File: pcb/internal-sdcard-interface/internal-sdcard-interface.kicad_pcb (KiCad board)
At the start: 2 copper layers, 219 x 88 mm, 77 parts, among them J1 EXPANSION BOARD, J2 POWER, J3 TERMINAL, J5 SDCARD, U1 74HC04, U10 74HC173, U11 74HC245, U12 74HC157, U17 74HC85, U18 74HC00, U19 74HC00, U2 CY62256-70PC, U20 74HC02, U21 74HC123, U23 74HC163, U24 74HC138, U25 74HC138, U26 74HC32, U27 74HC00, U29 74HC165, U3 74HC00, U30 74HC595, U31 74HC273, U32 74HC273, U33 SST39SF010, U34 CY62128ELL-45SXI, U4 CY62256-70PC, U5 74HC74, U6 74HC74, U7 74HC32, U8 74HC688, U9 74HC32, X1 16MHz

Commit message: Updating session
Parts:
- added G***: LOGO, components:hcm_logo, F.Cu at (253.2, 133.1)
- moved C10 10.9 mm to (130.8, 122.0), turned to -90 degrees
- moved J2 2.79 mm to (254.0, 85.1), turned to 0 degrees
- moved C3 2.29 mm to (67.3, 123.2)
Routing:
- net D0: track 0.00 -> 414.0 mm, vias 0 -> 5
- net D1: track 0.00 -> 384.9 mm, vias 0 -> 4
- net ~{WR}: track 0.00 -> 360.9 mm, vias 0 -> 2
- net D2: track 0.00 -> 332.0 mm, vias 0 -> 1
- net D6: track 0.00 -> 293.3 mm, vias 0 -> 2
- net ~{RES}: track 0.00 -> 292.3 mm, vias 0 -> 4
- net ~{RD}: track 0.00 -> 277.3 mm, vias 0 -> 2
- net D3: track 0.00 -> 275.8 mm, vias 0 -> 4
- net D4: track 0.00 -> 271.4 mm, vias 0 -> 2
- net D7: track 0.00 -> 265.1 mm, vias 0 -> 3
- net D5: track 0.00 -> 251.5 mm, vias 0 -> 2
- net Net-(U6B-C): track 0.00 -> 229.5 mm, vias 0 -> 3
- net Net-(U6A-C): track 0.00 -> 227.3 mm, vias 0 -> 4
- net CA15: track 0.00 -> 223.5 mm, vias 0 -> 3
- net A3: track 0.00 -> 221.9 mm, vias 0 -> 2
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- added copper zone on F.Cu, net GND
- added copper zone on B.Cu, net VCC
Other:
- board text added: "SDRE - MINIBOARD rev0 SD-CARD INTERFACE / 64 KiB - RAM-EXPANSION"
- board text removed: "MINIBOARD SD-CARD INTERFACE / 64 KiB - RAM-EXPANSION"

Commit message: Finalizing rev0
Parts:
- added REF**: OSHW-Logo2_7.3x6mm_SilkScreen, Symbol:OSHW-Logo2_7.3x6mm_SilkScreen, F.Cu at (253.5, 125.0)
- moved C10 12.1 mm to (135.6, 133.1), turned to 0 degrees
- moved C3 3.22 mm to (65.4, 125.7)
- renumbered G*** to G001
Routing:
- net GND: track 1846.3 -> 1693.2 mm, vias 2 -> 7
- net Net-(U6B-C): track 229.5 -> 202.7 mm, vias 3 -> 5
- net D0: track 414.0 -> 432.2 mm, vias 5 -> 4
- net VCC: track 1411.9 -> 1421.2 mm, vias 0 -> 1
- net CLK: track 124.2 -> 133.3 mm, vias 3 -> 5
- net CA6: track 193.5 -> 189.6 mm
- net ~{CLKSTART_DB}: track 137.4 -> 139.8 mm
- net CA4: track 169.0 -> 171.0 mm
- net RAMS2: track 158.1 -> 160.1 mm, vias 1 -> 3
- net CA10: track 172.6 -> 174.2 mm
- net CA13: track 198.4 -> 199.9 mm
- net CA11: track 191.3 -> 192.7 mm
- net CA8: track 190.5 -> 189.1 mm
- net ~{S13}: track 181.6 -> 182.9 mm
- net A14: track 170.3 -> 171.5 mm, vias 1 -> 3
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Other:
- board text added: "CLK"
- board text added: "Designed by Ivo Filot (2024) Sources: https://github.com/ifilot/p2000t-sdcard"
- board text added: "LEDBANK"
- board text added: "MISO"
- board text added: "MOSI"
- board text added: "VCC"
- board text added: "~{CS}"

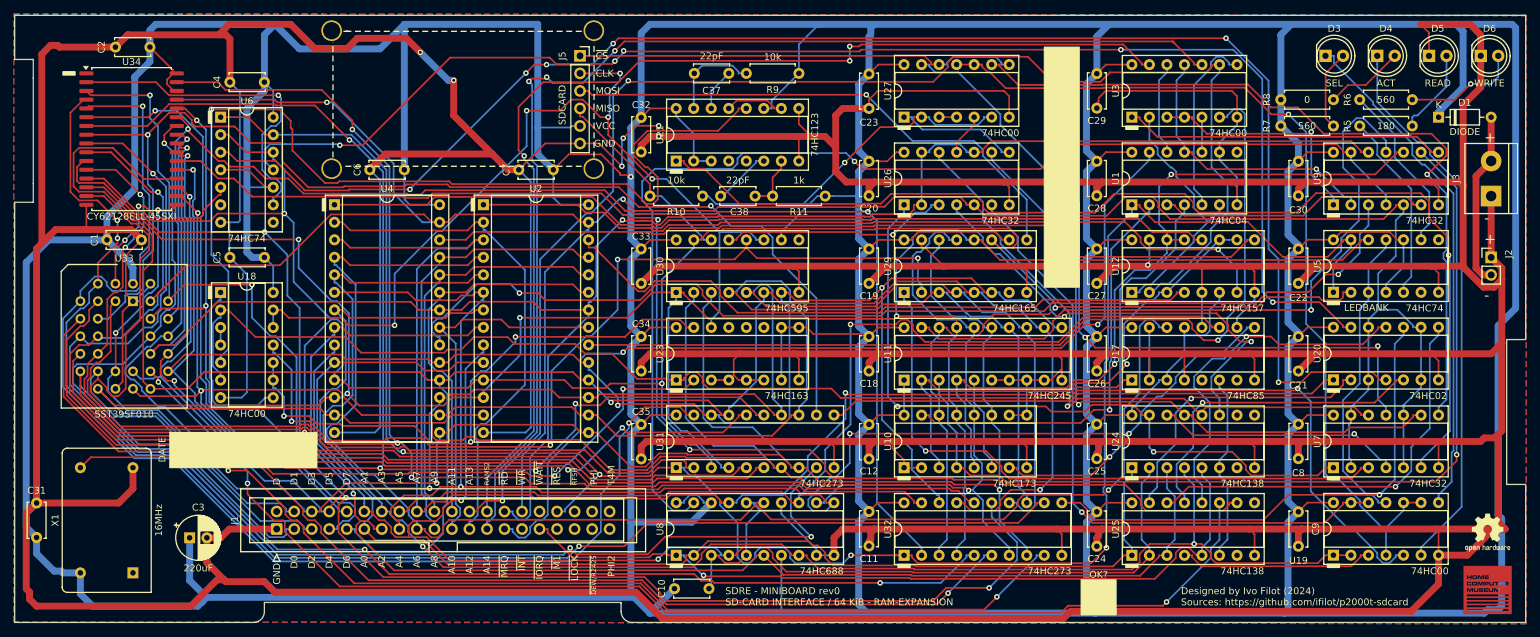
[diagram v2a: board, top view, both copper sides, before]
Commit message: Small revision of miniboard and enabling autoboot function
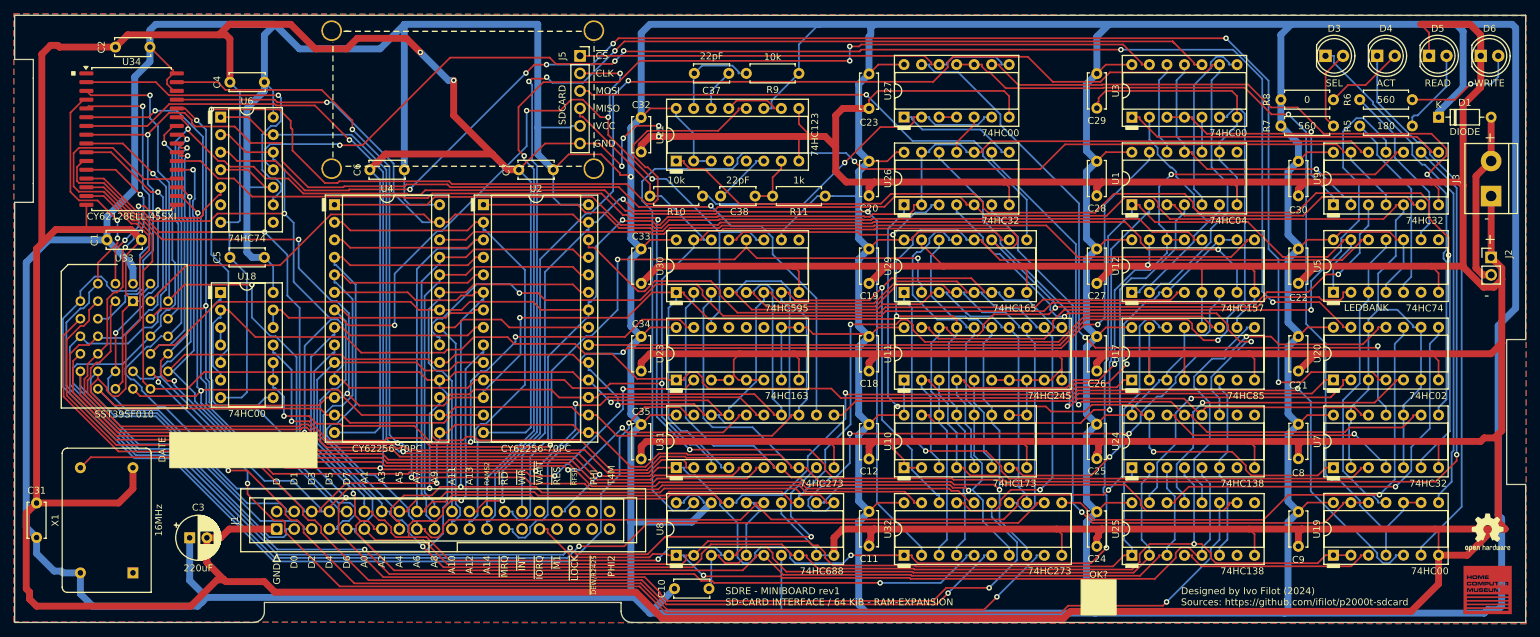
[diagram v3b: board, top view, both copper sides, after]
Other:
- board text added: "SDRE - MINIBOARD rev1 SD-CARD INTERFACE / 64 KiB - RAM-EXPANSION"
- board text removed: "SDRE - MINIBOARD rev0 SD-CARD INTERFACE / 64 KiB - RAM-EXPANSION"
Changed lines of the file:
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@@
 		(tags "THT DIP DIL PDIP 2.54mm 7.62mm 300mil Socket")
 		(property "Reference" "U19"
-			(at -0.782 -5.08 0)
+			(at 3.79 -2.413 90)
 			(layer "F.SilkS")
 			(effects
@@
 		(tags "C Disc series Radial pin pitch 5.00mm  diameter 5mm width 2.5mm Capacitor")
 		(property "Reference" "C9"
-			(at 2.5 -2.5 90)
+			(at 6.945 0 180)
 			(layer "F.SilkS")
 			(effects
@@
 		(property "Value" "CY62256-70PC"
 			(at 7.62 35.35 0)
-			(layer "F.Fab")
+			(layer "F.SilkS")
 			(effects
 				(font
@@
 		(property "Value" "CY62256-70PC"
 			(at 7.62 35.35 0)
-			(layer "F.Fab")
+			(layer "F.SilkS")
 			(effects
 				(font
@@
 	)
 	(gr_rect
-		(start 46.99 58.166)
+		(start 48.26 58.166)
 		(end 48.768 58.674)
 		(stroke
@@
 	)
 	(gr_rect
-		(start 189.23 54.61)
-		(end 194.31 89.408)
-		(stroke
-			(width 0.15)
-			(type solid)
-		)
-		(fill solid)
-		(layer "F.SilkS")
-	)
-	(gr_rect
 		(start 168.021 78.74)
 		(end 169.799 79.248)
@@
 		)
 	)
-	(gr_text "SDRE - MINIBOARD rev0\nSD-CARD INTERFACE / 64 KiB - RAM-EXPANSION"
+	(gr_text "SDRE - MINIBOARD rev1\nSD-CARD INTERFACE / 64 KiB - RAM-EXPANSION"
 		(at 143.002 135.636 0)
 		(layer "F.SilkS")
